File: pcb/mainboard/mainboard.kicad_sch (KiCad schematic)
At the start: 37 parts, among them J1 V_IN, SW1 RES_BUT, SW2 BOOT_SW, U1 STM32G474RETx, U2 TPS54331DDA, Y1 8MHz

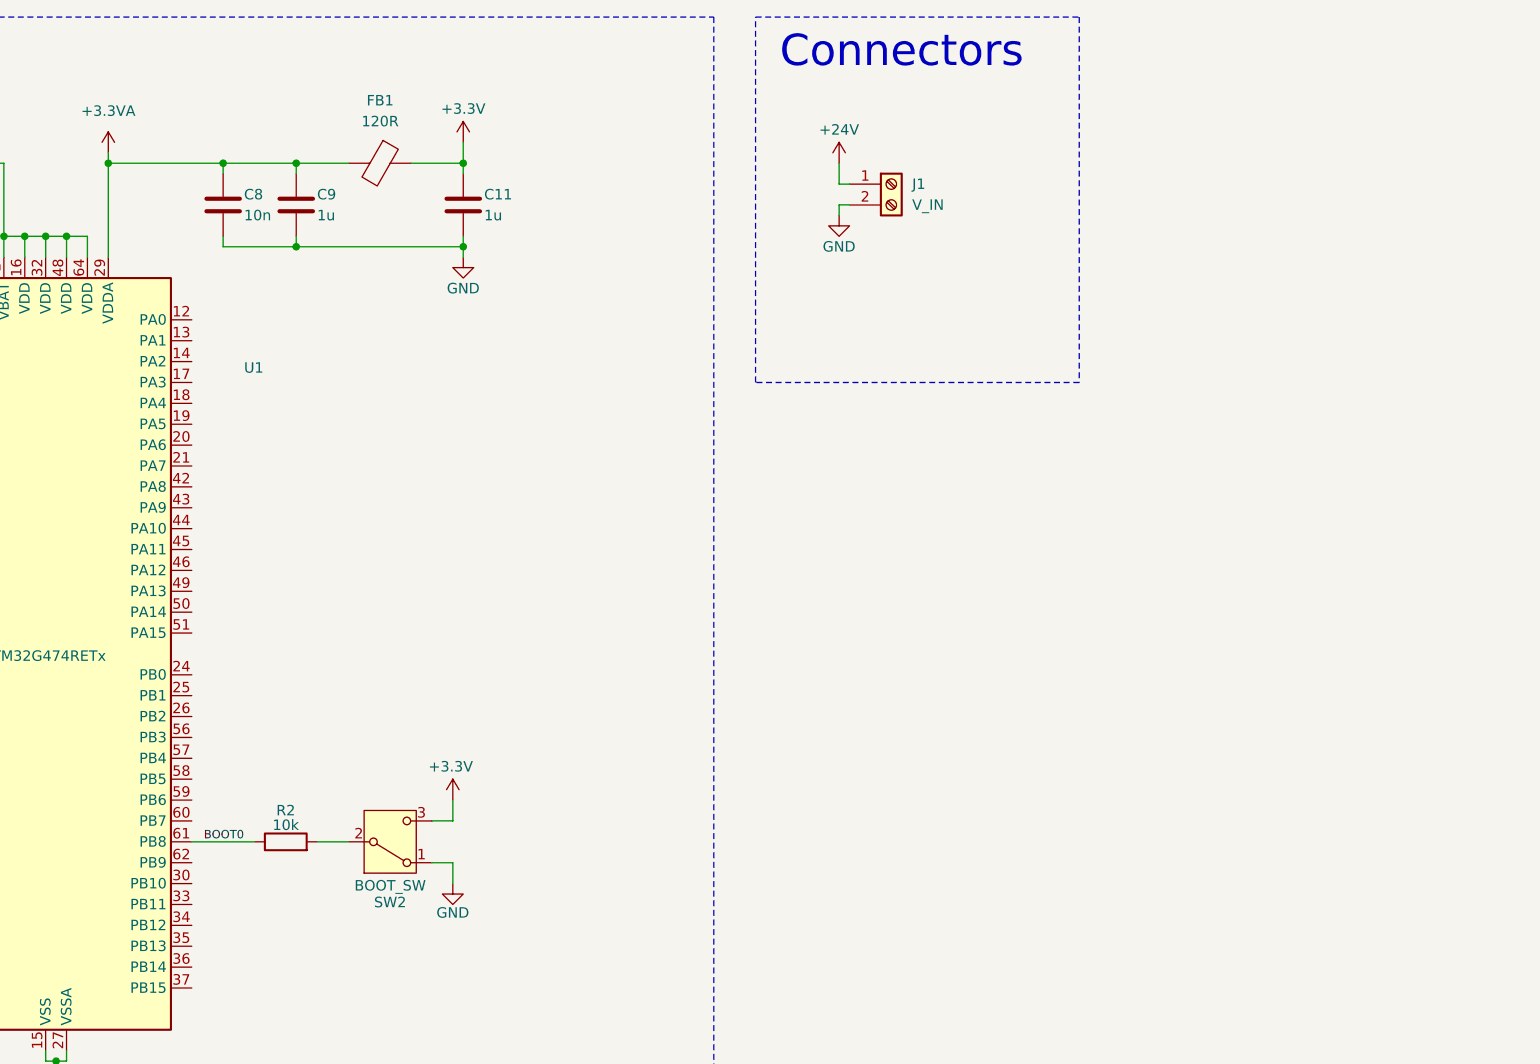
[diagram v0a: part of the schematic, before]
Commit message: Add USB C port and integrate it with uC
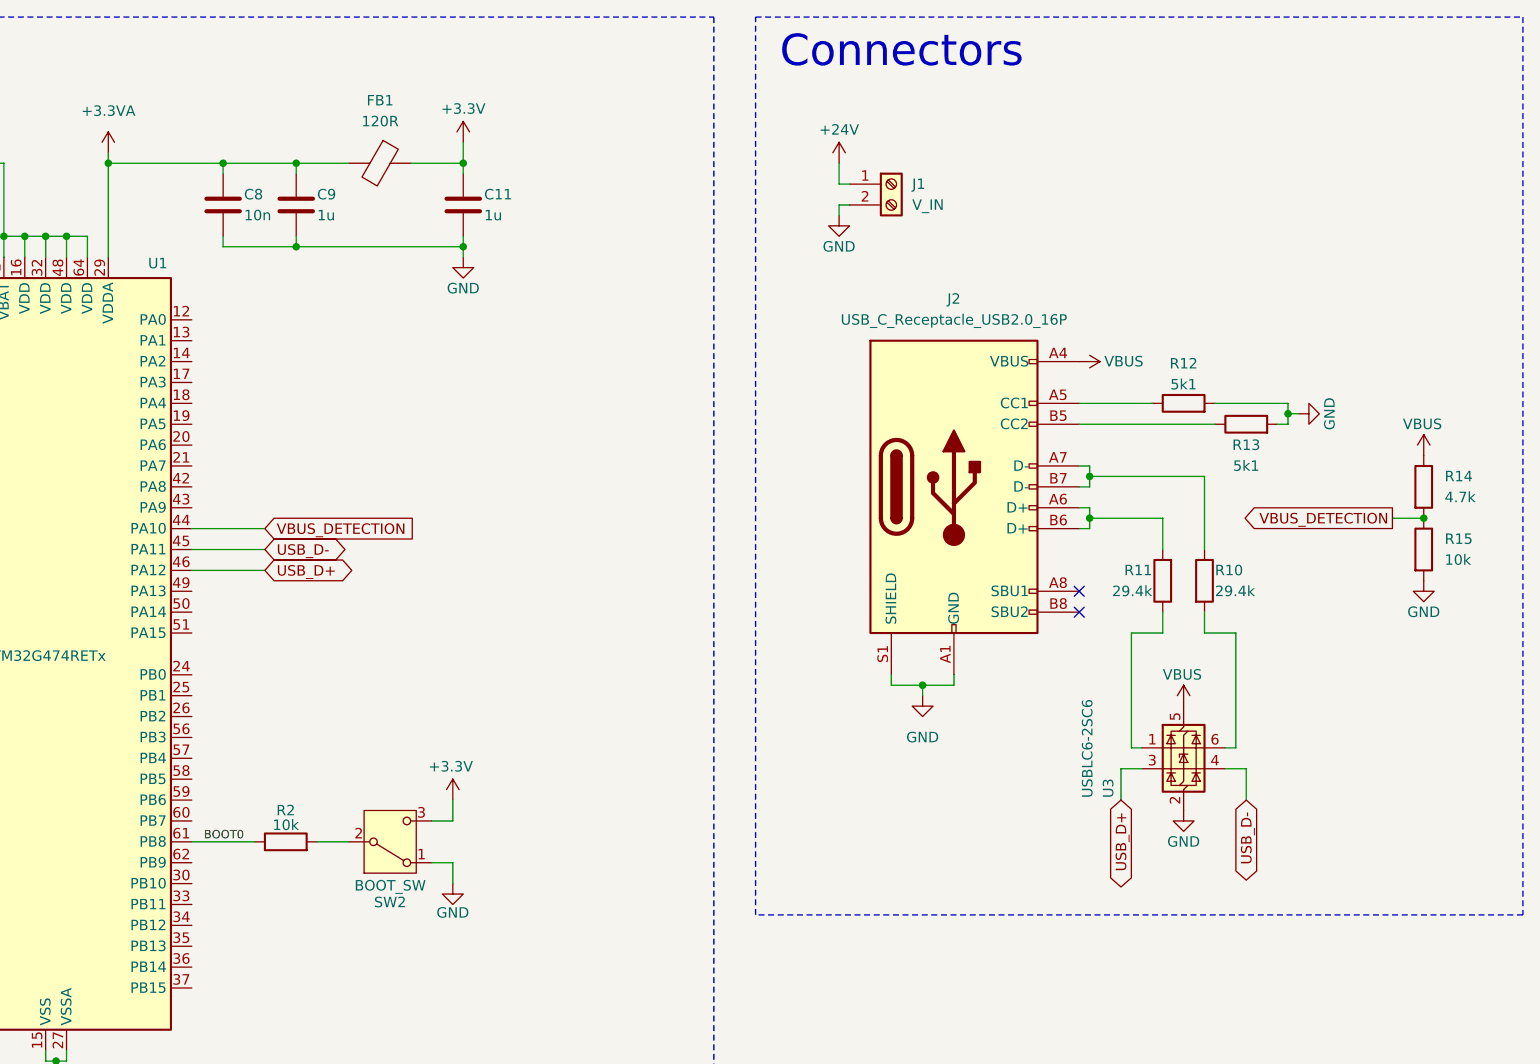
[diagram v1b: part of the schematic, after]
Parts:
- added J2: USB_C_Receptacle_USB2.0_16P, symbol Connector:USB_C_Receptacle_USB2.0_16P
- added R10, R11: 29.4k, symbol Device:R
- added R12, R13: 5k1, symbol Device:R
- added R14: 4.7k, symbol Device:R
- added R15: 10k, symbol Device:R
- added U3: USBLC6-2SC6, Package_TO_SOT_SMD:SOT-23-6, symbol Power_Protection:USBLC6-2SC6
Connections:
- net GND: now also J2.A1 (GND), J2.A12 (GND), J2.B1 (GND), J2.B12 (GND), J2.S1 (SHIELD), R12.2, R13.2, R15.2, U3.2 (GND)
- net VBUS_DETECTION: now reaches U1.44 (PA10)
- net VBUS_DETECTION: now also R14.2, R15.1
- net USB_D-: now reaches U1.45 (PA11)
- net USB_D-: now also U3.4 (I/O2)
- net USB_D+: now reaches U1.46 (PA12)
- net USB_D+: now also U3.3 (I/O2)
- new net: J2.B5 (CC2), R13.1
- new net: R11.1, U3.1 (I/O1)
- new net: R10.2, U3.6 (I/O1)
- new net: J2.A7 (D-), J2.B7 (D-), R10.1
- new net: J2.A5 (CC1), R12.1
- new net: J2.A6 (D+), J2.B6 (D+), R11.2
- new net VBUS: J2.A4 (VBUS), J2.A9 (VBUS), J2.B4 (VBUS), J2.B9 (VBUS), R14.1, U3.5 (VBUS)
- no-connect marks 0 -> 2

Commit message: add stepsticks
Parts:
- removed J2: USB_C_Receptacle_USB2.0_16P, symbol Connector:USB_C_Receptacle_USB2.0_16P
- removed R10, R11: 29.4k, symbol Device:R
- removed R12, R13: 5k1, symbol Device:R
- removed R14: 4.7k, symbol Device:R
- removed R15: 10k, symbol Device:R
- removed U3: USBLC6-2SC6, Package_TO_SOT_SMD:SOT-23-6, symbol Power_Protection:USBLC6-2SC6
- removed Y1: 8MHz, symbol Device:Crystal
- added C21, C22: 100n, symbol Device:C_Polarized
- added C23, C24: 4.7u, symbol Device:C
- added J2: SWD, CONN_3220-10-0100-00_CNC, symbol CONN_3220-10-0100-00_CNC:3220-10-0100-00
- added J3: Conn_01x10, symbol Connector_Generic:Conn_01x10
- added J4: M1, symbol Connector_Generic:Conn_01x04
- added J5: M2, symbol Connector_Generic:Conn_01x04
- added U3, U4: TMC2208_SILENTSTEPSTICK, TMC2208_SILENTSTEPSTICK:MODULE_TMC2208_SILENTSTEPSTICK, symbol TMC2208_SILENTSTEPSTICK:TMC2208_SILENTSTEPSTICK
- added Y1: 16MHz, symbol Device:Crystal_GND23
- C7: value 0.1u -> 100n
- U2: footprint DDA8_3X2P13 -> (none)
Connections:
- net +24V: now also C21.1, C22.1, U3.JP2_1 (VM), U4.JP2_1 (VM)
- net +3.3V: now also C23.1, C24.1, J3.2 (Pin_2)
- net +3.3VA: now also U1.28 (VREF+)
- net GND: now also C21.2, C22.2, C23.2, C24.2, J2.3, J2.4, J3.1 (Pin_1), U3.JP1_4 (PDN/UART1), U3.JP1_5 (PDN/UART2), U3.JP1_6 (MS2), U3.JP1_7 (MS1), U4.JP1_4 (PDN/UART1), U4.JP1_5 (PDN/UART2), U4.JP1_6 (MS2), U4.JP1_7 (MS1), U4.JP2_2 (GND), U4.JP2_8 (GND), Y1.2, Y1.3
- net RESET: now also J2.1
- net at C6.1, U1.6 (PF1): now also Y1.4
- net DIR_2: now reaches U1.10 (PC2)
- net DIR_2: now also U4.JP1_1 (DIR)
- net STEP_2: now reaches U1.11 (PC3)
- net STEP_2: now also U4.JP1_2 (STEP)
- net OLED_RESET: now reaches U1.12 (PA0)
- net OLED_RESET: now also J3.6 (Pin_6)
- net OLED_DC: now reaches U1.13 (PA1)
- net OLED_DC: now also J3.5 (Pin_5)
- net OLED_CS: now reaches U1.18 (PA4)
- net OLED_CS: now also J3.7 (Pin_7)
- net M_ENABLE: now reaches U1.20 (PA6)
- net M_ENABLE: now also U3.JP1_8 (EN), U4.JP1_8 (EN)
- net ENC_BTN: now reaches U1.21 (PA7)
- net ENC_BTN: now also J3.8 (Pin_8)
- net OLED_SCK: now reaches U1.35 (PB13)
- net OLED_SCK: now also J3.4 (Pin_4)
- net OLED_MOSI: now reaches U1.37 (PB15)
- net OLED_MOSI: now also J3.3 (Pin_3)
- net ENC_SIG_A: now reaches U1.42 (PA8)
- net ENC_SIG_A: now also J3.9 (Pin_9)
- net ENC_SIG_B: now reaches U1.43 (PA9)
- net ENC_SIG_B: now also J3.10 (Pin_10)
- net SWDIO: now reaches U1.49 (PA13)
- net SWDIO: now also J2.2
- net at C5.1, U1.5 (PF0): now also Y1.1
- net SWCLK: now reaches U1.50 (PA14)
- net SWCLK: now also J2.6
- net DIR_1: now reaches U1.8 (PC0)
- net DIR_1: now also U3.JP1_1 (DIR)
- net STEP_1: now reaches U1.9 (PC1)
- net STEP_1: now also U3.JP1_2 (STEP)
- net USB_D+: no longer names the net of U1.46 (PA12)
- net USB_D-: no longer names the net of U1.45 (PA11)
- net VBUS_DETECTION: no longer names the net of U1.44 (PA10)
- new net: U3.JP2_2 (GND), U3.JP2_8 (GND)
- new net M1OA1: J4.1 (Pin_1), U3.JP2_4 (OA1)
- new net M1OA2: J4.2 (Pin_2), U3.JP2_3 (OA2)
- new net M1OB1: J4.3 (Pin_3), U3.JP2_5 (OB1)
- new net M1OB2: J4.4 (Pin_4), U3.JP2_6 (OB2)
- new net M2OA1: J5.1 (Pin_1), U4.JP2_4 (OA1)
- new net M2OA2: J5.2 (Pin_2), U4.JP2_3 (OA2)
- new net M2OB1: J5.3 (Pin_3), U4.JP2_5 (OB1)
- new net M2OB2: J5.4 (Pin_4), U4.JP2_6 (OB2)
- no-connect marks 2 -> 11
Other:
- note added: "Stepsticks"
- moved on the sheet: C5, C6, J1

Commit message: add IDA
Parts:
- added C25: 100n, Capacitor_SMD:C_0603_1608Metric_Pad1.08x0.95mm_HandSolder, symbol Device:C
- added J6: INA_IN, symbol Connector:Screw_Terminal_01x02
- added R10, R9: 10k, symbol Device:R
- added R11: 100, symbol Device:R
- added U5: INA219AxD, Package_SO:SOIC-8_3.9x4.9mm_P1.27mm, symbol Sensor_Energy:INA219AxD
- C1, C2, C3, C4, C7: footprint (none) -> Capacitor_SMD:C_0603_1608Metric_Pad1.08x0.95mm_HandSolder
- C23, C24: value 4.7u -> 100n; footprint (none) -> Capacitor_SMD:C_0603_1608Metric_Pad1.08x0.95mm_HandSolder
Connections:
- net +3.3V: now also U3.JP2_7 (VIO), U4.JP2_7 (VIO), C25.1, R10.1, R9.1, U5.5 (VS)
- net GND: now also C25.2, U5.1 (A1), U5.2 (A0), U5.6 (GND)
- net INA_SCL: now reaches U1.51 (PA15)
- net INA_SCL: now also R10.2, U5.4 (SCL)
- net INA_SDA: now reaches U1.60 (PB7)
- net INA_SDA: now also R9.2, U5.3 (SDA)
- new net INA+: J6.1 (Pin_1), R11.1, U5.8 (IN+)
- new net INA-: J6.2 (Pin_2), R11.2, U5.7 (IN-)
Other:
- note added: "INA219"
- moved on the sheet: C12, C13, C14, C15, C16, C17, C18, C19, C20, D1, J1, J2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

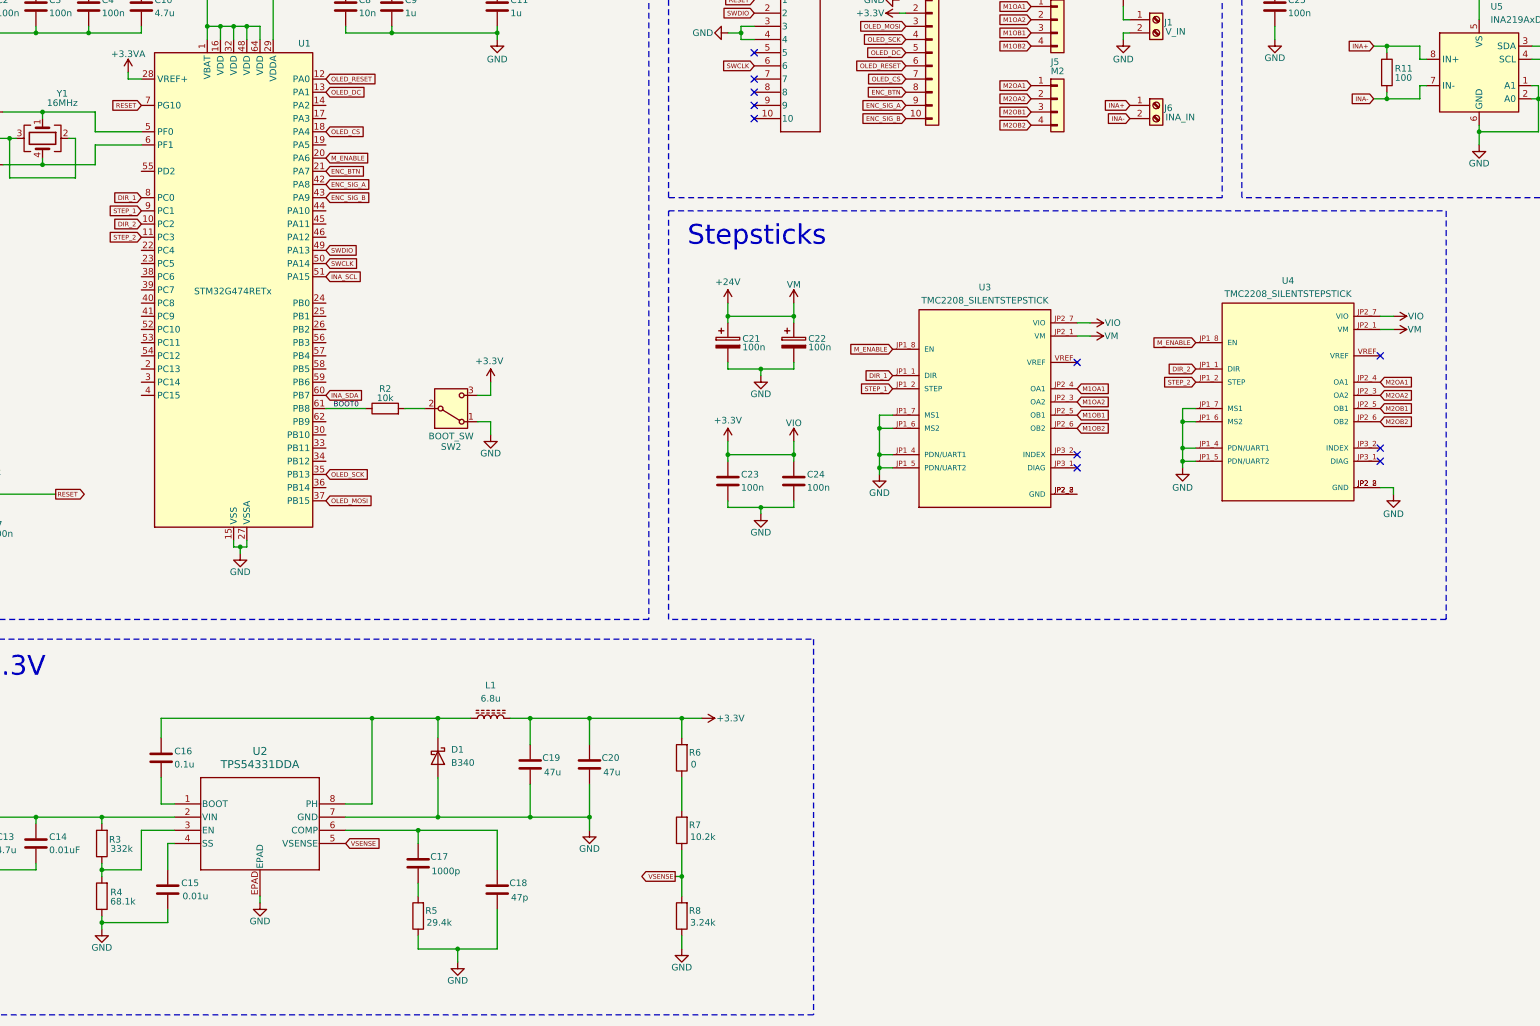
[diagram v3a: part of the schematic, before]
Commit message: Add TIP Voltage Control
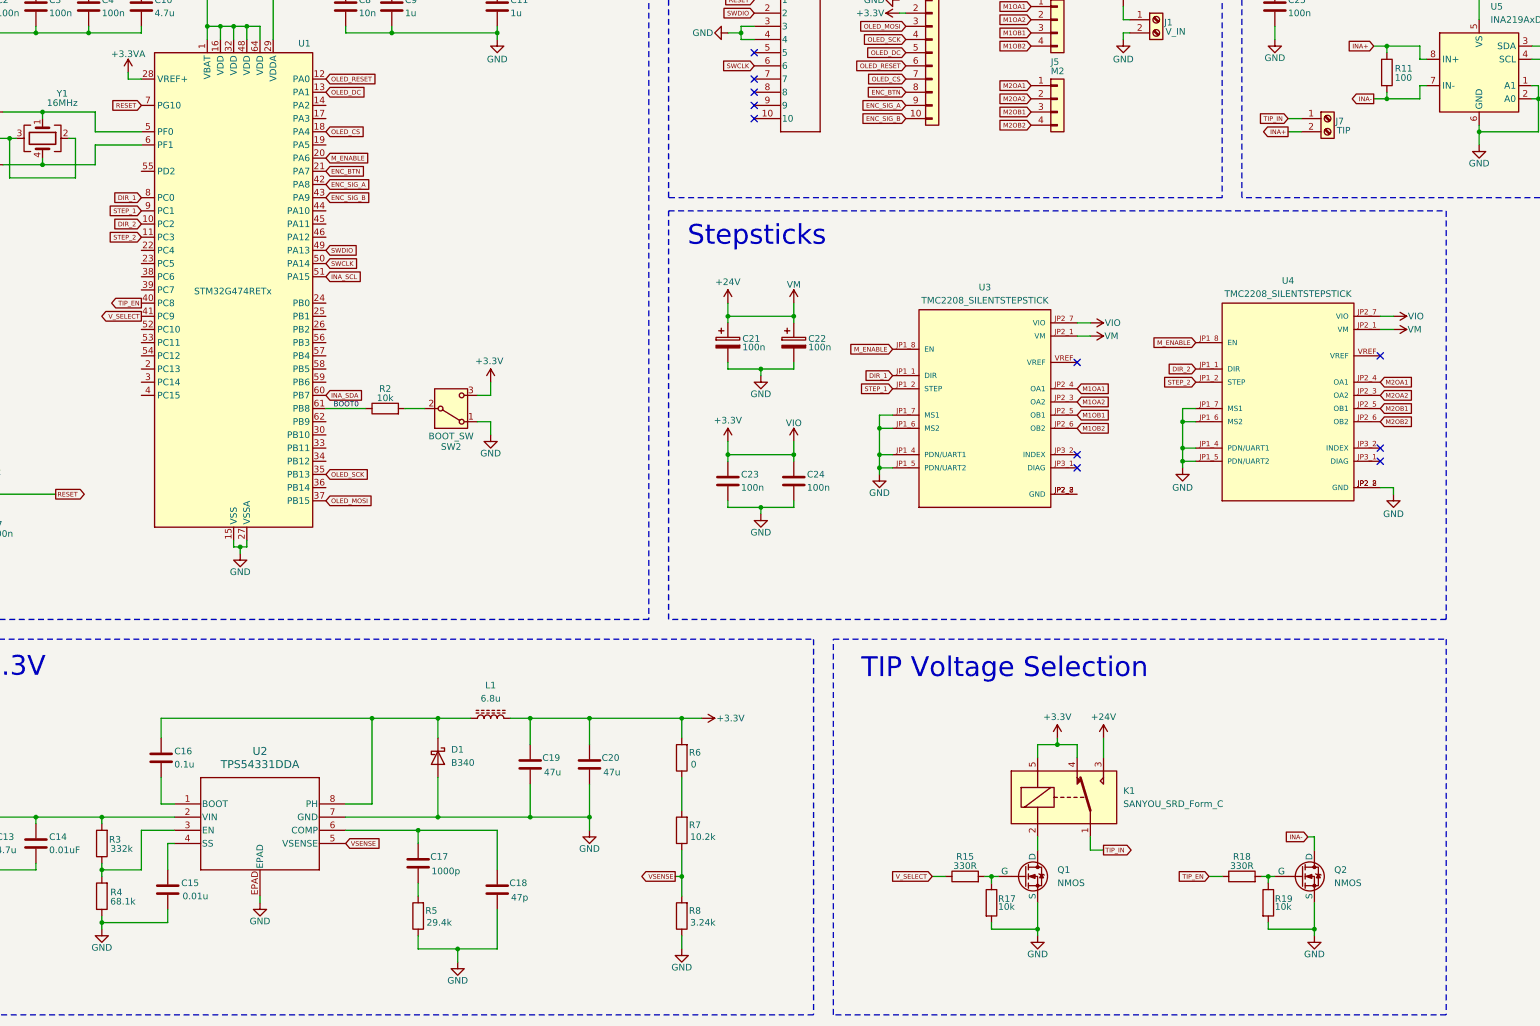
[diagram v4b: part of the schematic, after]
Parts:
- removed J6: INA_IN, symbol Connector:Screw_Terminal_01x02
- added J7: TIP, symbol Connector:Screw_Terminal_01x02
- added K1: SANYOU_SRD_Form_C, Relay_THT:Relay_SPDT_SANYOU_SRD_Series_Form_C, symbol Relay:SANYOU_SRD_Form_C
- added Q1, Q2: NMOS, symbol Simulation_SPICE:NMOS
- added R15, R18: 330R, Resistor_SMD:R_0603_1608Metric_Pad0.98x0.95mm_HandSolder, symbol Device:R
- added R17, R19: 10k, Resistor_SMD:R_0603_1608Metric_Pad0.98x0.95mm_HandSolder, symbol Device:R
- C10, C11, C12, C13, C14, C15, C16, C17, C18, C19, C20, C5, C6, C8, C9: footprint (none) -> Capacitor_SMD:C_0603_1608Metric_Pad1.08x0.95mm_HandSolder
- FB1, R1, R10, R2, R3, R4, R5, R6, R7, R8, R9: footprint (none) -> Resistor_SMD:R_0603_1608Metric_Pad0.98x0.95mm_HandSolder
- J3: footprint (none) -> Connector_PinSocket_2.54mm:PinSocket_1x10_P2.54mm_Vertical
- J4, J5: footprint (none) -> Connector_PinSocket_2.54mm:PinSocket_1x04_P2.54mm_Vertical
- R11: footprint (none) -> Resistor_SMD:R_1206_3216Metric_Pad1.30x1.75mm_HandSolder
- SW1: footprint (none) -> Button_Switch_SMD:SW_Tactile_SPST_NO_Straight_CK_PTS636Sx25SMTRLFS
- SW2: footprint (none) -> Button_Switch_THT:SW_Slide_SPDT_Straight_CK_OS102011MS2Q
- Y1: footprint (none) -> Oscillator:Oscillator_SMD_Abracon_ASE-4Pin_3.2x2.5mm_HandSoldering
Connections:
- net +24V: now also K1.3
- net +3.3V: now also K1.4, K1.5
- net GND: now also Q1.3 (S), Q2.3 (S), R17.2, R19.2
- net INA+: now also J7.2 (Pin_2)
- net INA-: now also Q2.1 (D)
- net TIP_EN: now reaches U1.40 (PC8)
- net TIP_EN: now also R18.1
- net V_SELECT: now reaches U1.41 (PC9)
- net V_SELECT: now also R15.1
- new net: K1.2, Q1.1 (D)
- new net: Q2.2 (G), R18.2, R19.1
- new net: Q1.2 (G), R15.2, R17.1
- new net TIP_IN: J7.1 (Pin_1), K1.1
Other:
- note added: "TIP Voltage Selection"

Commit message: Create pcb
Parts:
- added H1, H2, H3, H4: MountingHole, MountingHole:MountingHole_3.2mm_M3, symbol Mechanical:MountingHole
- J1, J7: footprint (none) -> TerminalBlock:CONN_395011002_MOL
- L1: footprint (none) -> Inductor_SMD:IND_IHLP-2525CZ_VIS-M
- Q1, Q2: footprint (none) -> Package_TO_SOT_SMD:SOT-23_Handsoldering
- U2: footprint (none) -> Module:DDA8_3X2P13
- U3, U4: footprint TMC2208_SILENTSTEPSTICK:MODULE_TMC2208_SILENTSTEPSTICK -> Connector:MODULE_TMC2208_SILENTSTEPSTICK
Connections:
- no-connect marks 11 -> 39
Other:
- note added: "Holes"
